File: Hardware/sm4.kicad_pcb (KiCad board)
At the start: 4 copper layers, 65 x 50 mm, 91 parts, among them J1 Motor1, J2 Termination, J3 CAN bus, J4 Motor2, J5 I2C, J6 Power, J7 USB_C_Receptacle_USB2.0, J8 Conn_01x05_Male, Q1 NDT2955, SW1 RST_SW, SW2 BOOT_SW, U1 STM32F412RETx, U2 TMC2100-TA, U3 MCP2562-E-SN, U4 TMC2100-TA, U6 MCP1700-3302E_SOT23, U7 USBLC6-2SC6, Y1 25 MHz

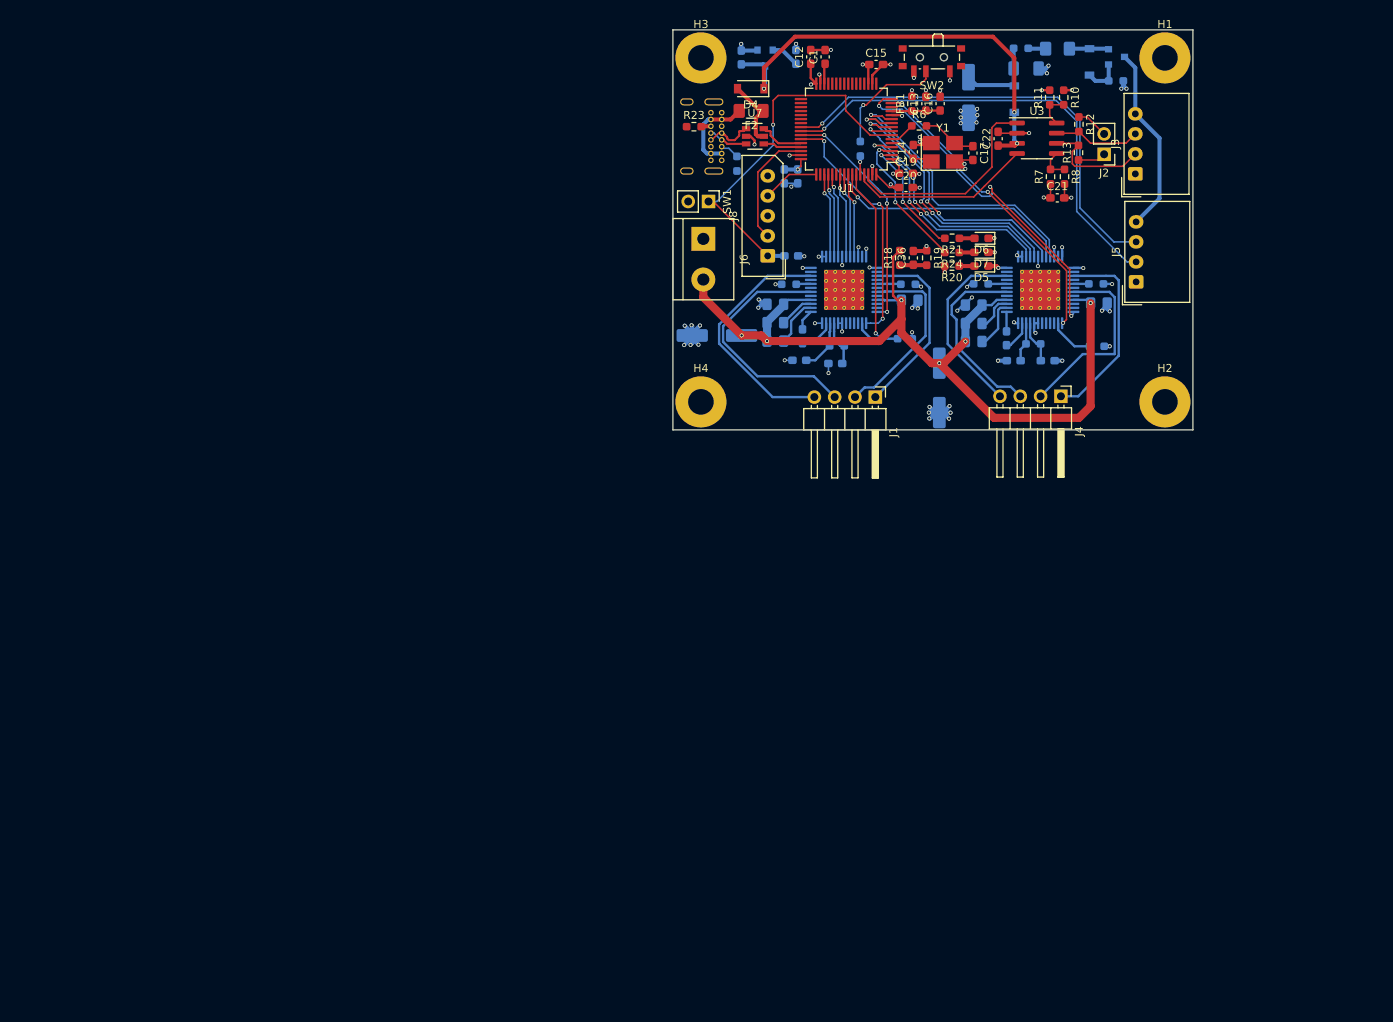
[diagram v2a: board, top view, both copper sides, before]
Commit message: Implement more of the second version of the PCB.
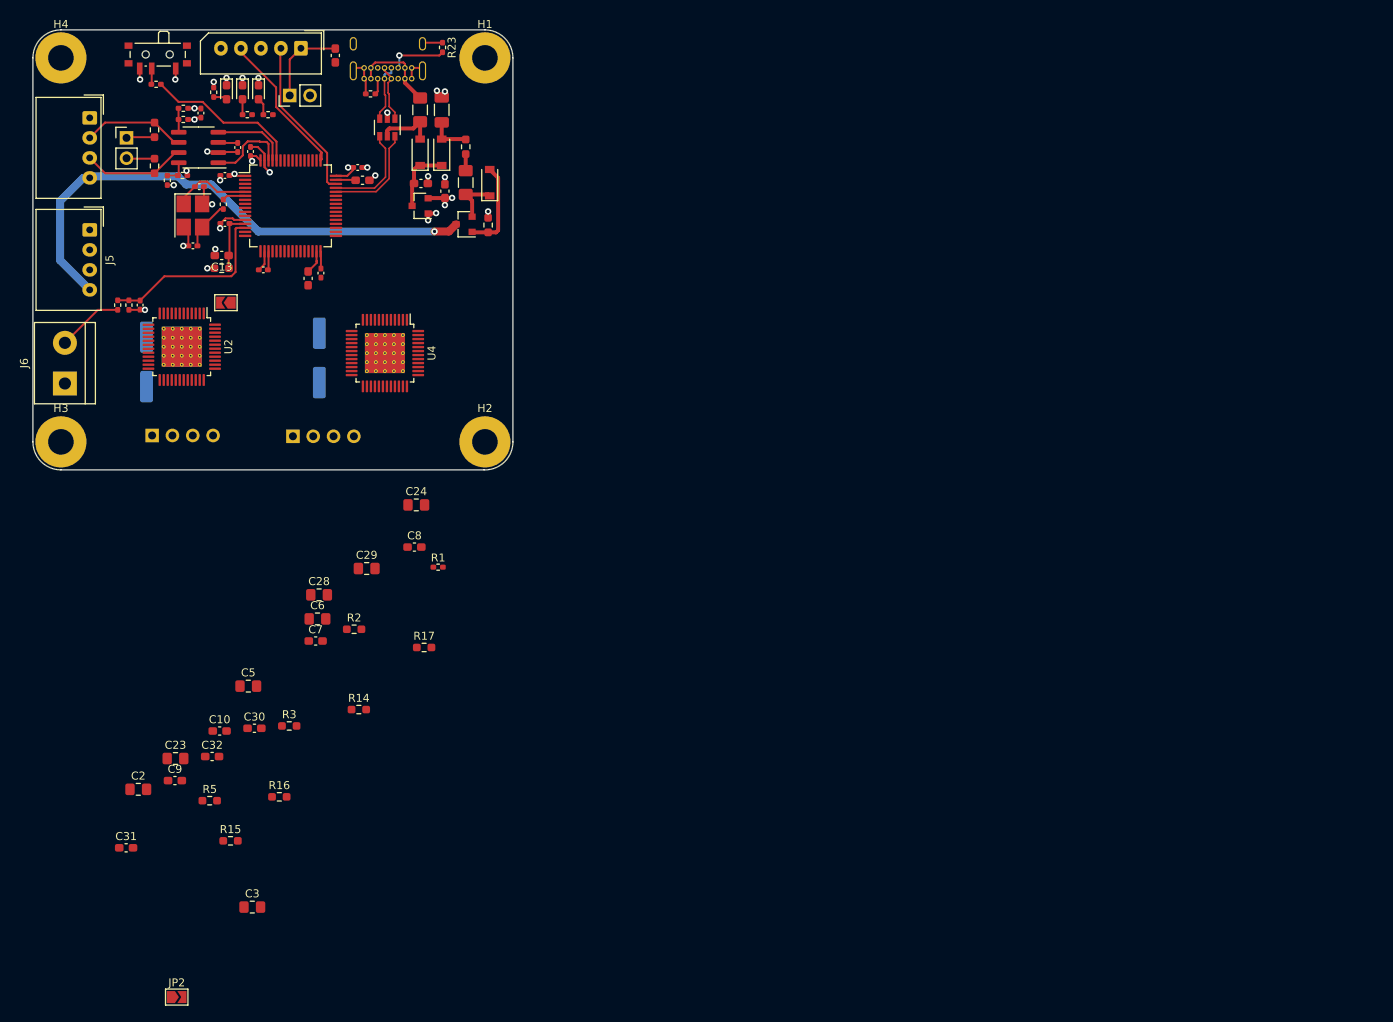
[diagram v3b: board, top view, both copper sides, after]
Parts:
- removed C27: 68u, Capacitor_SMD:C_Elec_6.3x7.7
- added C33: 2u2, Capacitor_SMD:C_0603_1608Metric_Pad1.08x0.95mm_HandSolder, F.Cu at (81.2, 68.8)
- added JP1: Jumper_2_Open, Jumper:SolderJumper-2_P1.3mm_Open_TrianglePad1.0x1.5mm, F.Cu at (64.1, 84.1)
- added JP2: Jumper_2_Open, Jumper:SolderJumper-2_P1.3mm_Open_TrianglePad1.0x1.5mm, F.Cu at (58.0, 170.9)
- C10, C11, C2, C23, C24, C25, C28, C29, C3, C30, C31, C32, C34, C35, C5, C6, C7, C8, C9, D1, D3, F1, FB2, Q1, R14, R15, R16, R17, R2, R3, R5, R9, U2, U4, U6: moved to F.Cu
- C12, C14, C15, C16, C17, C19, C20, C21, C22, C36: footprint Capacitor_SMD:C_0603_1608Metric_Pad1.08x0.95mm_HandSolder -> Capacitor_SMD:C_0402_1005Metric_Pad0.74x0.62mm_HandSolder
- C18: footprint Capacitor_SMD:C_0603_1608Metric_Pad1.08x0.95mm_HandSolder -> Capacitor_SMD:C_0402_1005Metric_Pad0.74x0.62mm_HandSolder; moved to F.Cu
- J1, J4: moved to B.Cu
- R1, R22, R4: footprint Resistor_SMD:R_0603_1608Metric_Pad0.98x0.95mm_HandSolder -> Resistor_SMD:R_0402_1005Metric_Pad0.72x0.64mm_HandSolder; moved to F.Cu
- R10, R11, R18, R19, R20, R21, R23, R24, R6, R7, R8: footprint Resistor_SMD:R_0603_1608Metric_Pad0.98x0.95mm_HandSolder -> Resistor_SMD:R_0402_1005Metric_Pad0.72x0.64mm_HandSolder
- U1: value STM32F412RETx -> STM32F405RGTx
- moved J5 131.0 mm to (47.1, 75.0), turned to 270 degrees
- moved J3 130.9 mm to (47.1, 61.0), turned to 270 degrees
- moved C31 127.2 mm to (51.6, 152.2), turned to 0 degrees
- moved J2 122.2 mm to (51.7, 63.5), turned to 0 degrees
- moved R16 120.6 mm to (70.8, 145.9), turned to 0 degrees
- moved R15 118.0 mm to (64.7, 151.4), turned to 0 degrees
- moved R12 115.7 mm to (55.2, 67.0)
- moved R13 115.5 mm to (55.2, 62.5)
- moved C23 112.6 mm to (57.8, 141.1)
- moved C32 111.8 mm to (62.4, 140.8), turned to 0 degrees
- moved R11 110.8 mm to (56.8, 68.8), turned to 270 degrees
- moved R10 110.6 mm to (58.7, 68.2), turned to 180 degrees
- moved R8 110.5 mm to (58.8, 59.8), turned to 0 degrees
- moved C30 109.3 mm to (67.7, 137.3)
- moved R7 108.6 mm to (58.8, 61.2), turned to 180 degrees
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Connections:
- R21 pad 2: STATUS -> (no net)
- R24 pad 2: ERR -> (no net)
- U1 pad 10: CFG02 -> (no net)
- U1 pad 11: DIR2 -> (no net)
- U1 pad 15: CFG52 -> (no net)
- U1 pad 16: CFG42 -> EN1
- U1 pad 2: STATUS -> (no net)
- U1 pad 20: (no net) -> REF1
- U1 pad 21: (no net) -> REF2
- U1 pad 22: (no net) -> ERR1
- U1 pad 23: (no net) -> MODE1
- U1 pad 29: (no net) -> SCL
- U1 pad 3: ERR -> (no net)
- U1 pad 30: Net-(C1-Pad1) -> SDA
- U1 pad 31: GND -> Net-(C1-Pad1)
- U1 pad 37: (no net) -> STEP1
- U1 pad 38: (no net) -> DIR1
- U1 pad 4: CFG32 -> (no net)
- U1 pad 40: SDA -> (no net)
- U1 pad 41: SCL -> STEP2
- U1 pad 42: CFG41 -> (no net)
- U1 pad 43: CFG51 -> (no net)
- U1 pad 47: GND -> Net-(C33-Pad1)
- U1 pad 51: CFG31 -> (no net)
- U1 pad 52: CFG21 -> (no net)
- U1 pad 53: CFG11 -> (no net)
- U1 pad 55: CFG01 -> (no net)
- U1 pad 56: STEP1 -> (no net)
- U1 pad 57: DIR1 -> (no net)
- U1 pad 58: STEP2 -> (no net)
- U1 pad 59: ERR1 -> (no net)
- U1 pad 8: CFG22 -> (no net)
- U1 pad 9: CFG12 -> (no net)
- U2 pad 24: CFG41 -> GND
- U2 pad 25: CFG51 -> +3V3
- U2 pad 29: (no net) -> EN1
- U2 pad 3: CFG31 -> Net-(JP1-Pad2)
- U2 pad 30: (no net) -> REF1
- U2 pad 4: CFG21 -> (no net)
- U2 pad 5: CFG11 -> MODE1
- U2 pad 7: CFG01 -> GND
- U4 pad 24: CFG42 -> GND
- U4 pad 25: CFG52 -> +3V3
- U4 pad 3: CFG32 -> Net-(JP2-Pad2)
- U4 pad 30: (no net) -> REF2
- U4 pad 4: CFG22 -> (no net)
- U4 pad 5: CFG12 -> MODE1
- U4 pad 7: CFG02 -> GND
- U4 pad 9: DIR2 -> (no net)
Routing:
- net VS1: track 111.1 -> 8.31 mm, vias 6 -> 0
- net GND: track 110.9 -> 51.2 mm, vias 78 -> 24
- net SCL: track 58.5 -> 0.00 mm, vias 1 -> 0
- net SDA: track 57.4 -> 0.00 mm, vias 1 -> 0
- net +5V: track 56.3 -> 10.8 mm, vias 3 -> 0
- net CFG42: track 43.5 -> 0.00 mm, vias 3 -> 0
- net VDC: track 23.6 -> 66.6 mm, vias 0 -> 1
- net CFG52: track 37.9 -> 0.00 mm, vias 3 -> 0
- net NRST: track 47.1 -> 10.8 mm, vias 1 -> 0
- net DIR2: track 35.8 -> 0.00 mm, vias 1 -> 0
- net CFG02: track 35.5 -> 0.00 mm, vias 3 -> 0
- net CFG12: track 33.5 -> 0.00 mm, vias 3 -> 0
- net CFG22: track 31.9 -> 0.00 mm, vias 3 -> 0
- net Net-(J1-Pad4): track 31.8 -> 0.00 mm
- net STEP2: track 31.7 -> 0.00 mm, vias 1 -> 0
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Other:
- board size 65 x 50 mm -> 60 x 55 mm

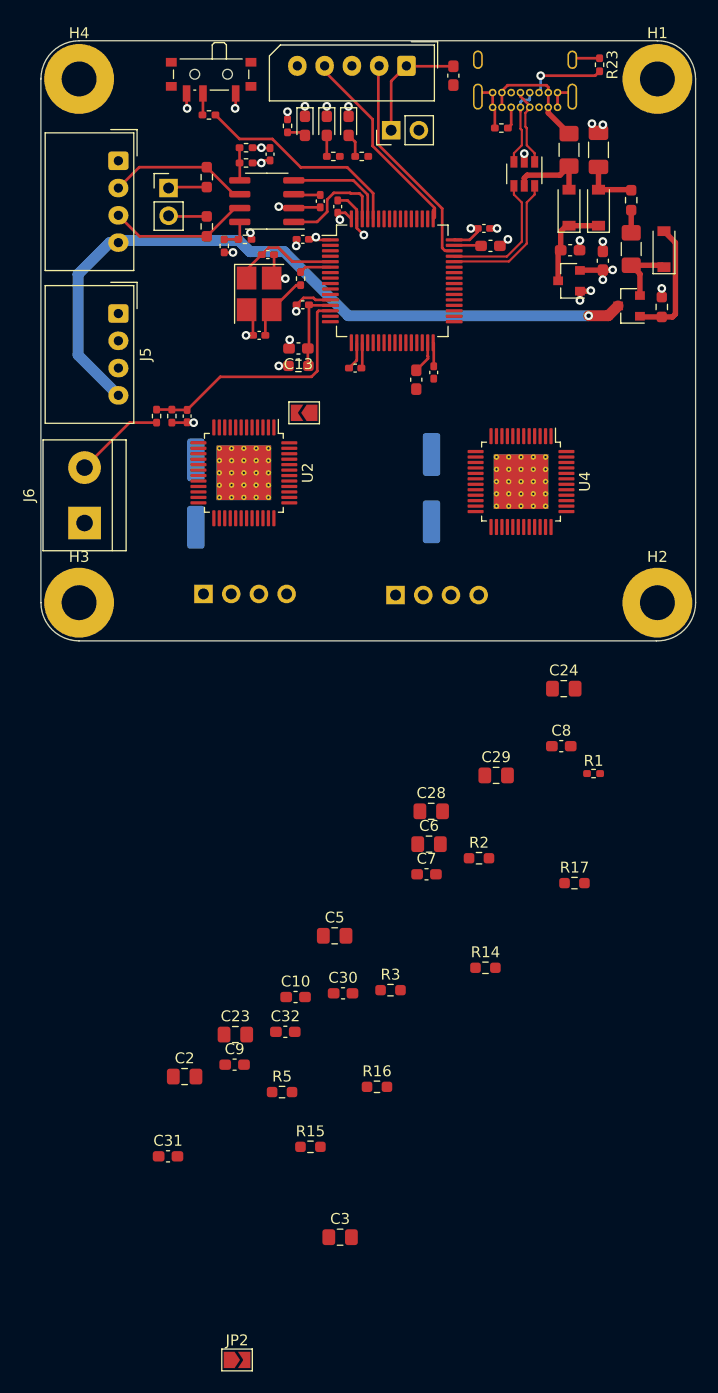
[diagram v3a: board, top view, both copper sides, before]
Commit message: Implement more of the second version of the PCB.
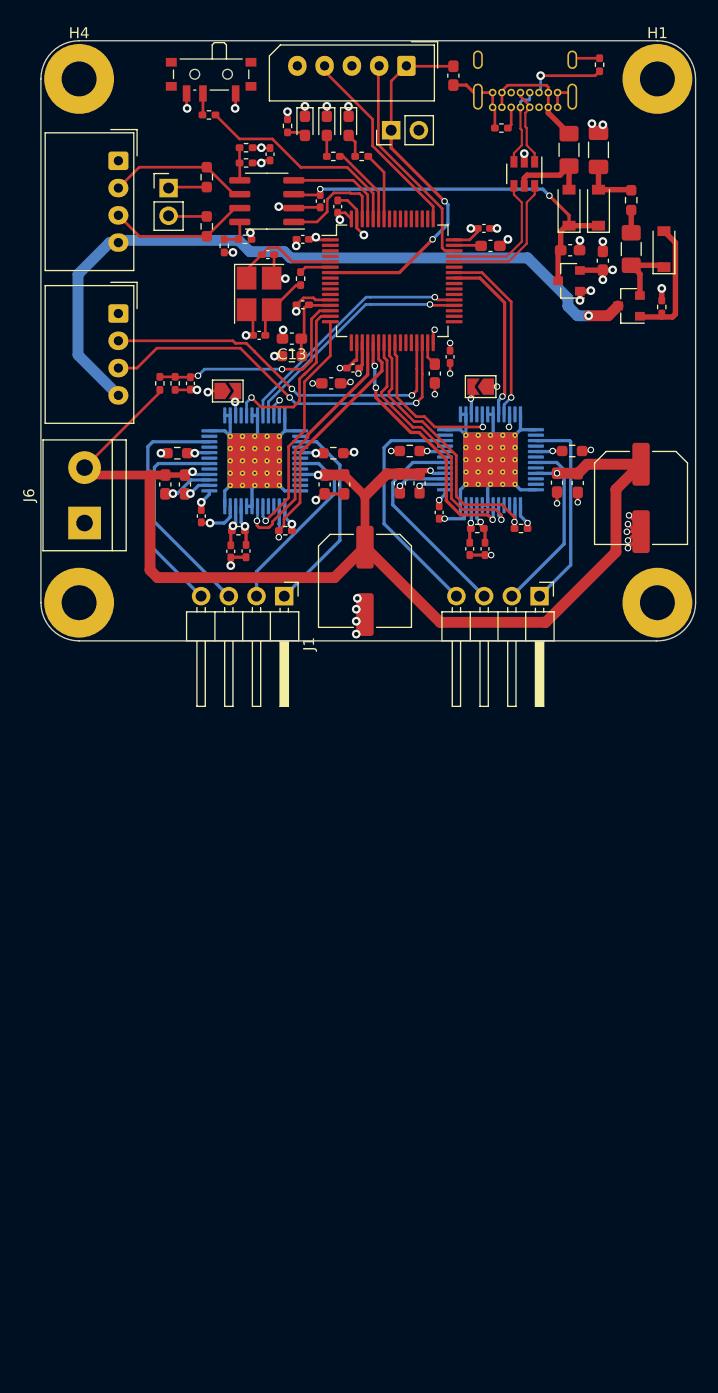
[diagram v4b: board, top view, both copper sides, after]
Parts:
- C10, C30, C31, C32, C7, C9: footprint Capacitor_SMD:C_0603_1608Metric_Pad1.08x0.95mm_HandSolder -> Capacitor_SMD:C_0402_1005Metric_Pad0.74x0.62mm_HandSolder
- C2, C23, C24, C28, C29, C3, C5, C6: footprint Capacitor_SMD:C_0805_2012Metric_Pad1.18x1.45mm_HandSolder -> Capacitor_SMD:C_0603_1608Metric_Pad1.08x0.95mm_HandSolder
- C26, C4, J1, J4: moved to F.Cu
- R14, R15, R2, R9: footprint Resistor_SMD:R_0603_1608Metric_Pad0.98x0.95mm_HandSolder -> Resistor_SMD:R_0402_1005Metric_Pad0.72x0.64mm_HandSolder
- U2, U4: moved to B.Cu
- moved JP2 92.0 mm to (80.3, 81.7), turned to 180 degrees
- moved C3 70.8 mm to (51.4, 90.7), turned to 270 degrees
- moved C31 64.0 mm to (76.5, 93.2), turned to 270 degrees
- moved R16 61.0 mm to (88.7, 87.6), turned to 180 degrees
- moved R5 59.3 mm to (52.5, 87.8)
- moved R15 58.7 mm to (80.0, 94.7), turned to 180 degrees
- moved C2 54.3 mm to (53.2, 90.7), turned to 270 degrees
- moved C23 53.3 mm to (74.7, 90.6), turned to 270 degrees
- moved C9 50.4 mm to (54.7, 93.6), turned to 270 degrees
- moved R3 49.5 mm to (66.8, 87.8), turned to 180 degrees
- moved C32 47.4 mm to (79.3, 96.6), turned to 270 degrees
- moved C30 42.8 mm to (80.7, 96.6), turned to 270 degrees
- moved R17 42.4 mm to (73.8, 87.6)
- moved C5 41.4 mm to (67.8, 90.7), turned to 270 degrees
- moved C10 41.3 mm to (57.4, 96.8), turned to 270 degrees
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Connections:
- R21 pad 2: (no net) -> STATUS
- R24 pad 2: (no net) -> ERR
- U1 pad 15: (no net) -> MODE1
- U1 pad 23: MODE1 -> EN2
- U1 pad 24: (no net) -> ERR2
- U1 pad 25: (no net) -> MODE2
- U1 pad 36: (no net) -> DIR1
- U1 pad 38: DIR1 -> (no net)
- U1 pad 42: (no net) -> DIR2
- U1 pad 58: (no net) -> ERR
- U1 pad 59: (no net) -> STATUS
- U4 pad 29: (no net) -> EN2
- U4 pad 5: MODE1 -> MODE2
- U4 pad 9: (no net) -> DIR2
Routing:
- net VS1: track 8.31 -> 119.5 mm, vias 0 -> 4
- net GND: track 51.2 -> 153.9 mm, vias 24 -> 46
- net SDA: track 0.00 -> 35.9 mm, vias 0 -> 2
- net SCL: track 0.00 -> 34.0 mm, vias 0 -> 2
- net ERR2: track 0.00 -> 26.0 mm, vias 0 -> 1
- net +5V: track 10.8 -> 36.0 mm, vias 0 -> 2
- net ERR1: track 0.00 -> 24.8 mm, vias 0 -> 1
- net EN2: track 0.00 -> 24.8 mm, vias 0 -> 1
- net REF2: track 0.00 -> 24.0 mm, vias 0 -> 3
- net REF1: track 0.00 -> 23.7 mm, vias 0 -> 1
- net NRST: track 10.8 -> 34.2 mm, vias 0 -> 2
- net STEP1: track 0.00 -> 22.9 mm, vias 0 -> 1
- net Net-(J4-Pad4): track 0.00 -> 22.2 mm
- net EN1: track 0.00 -> 22.1 mm, vias 0 -> 1
- net DIR1: track 0.00 -> 22.0 mm, vias 0 -> 1
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
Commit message: Finalize first HW version. Update firmware project.
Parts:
- removed D1: 4V7, Diode_SMD:D_SOD-123
- removed R9: 10k, Resistor_SMD:R_0402_1005Metric_Pad0.72x0.64mm_HandSolder
- added C27: 10u, Capacitor_SMD:C_1206_3216Metric_Pad1.33x1.80mm_HandSolder, F.Cu at (94.9, 85.9)
- added C37: 10u, Capacitor_SMD:C_1206_3216Metric_Pad1.33x1.80mm_HandSolder, F.Cu at (94.9, 93.6)
- added C38: 10u, Capacitor_SMD:C_1206_3216Metric_Pad1.33x1.80mm_HandSolder, F.Cu at (71.5, 103.7)
- added C39: 10u, Capacitor_SMD:C_1206_3216Metric_Pad1.33x1.80mm_HandSolder, F.Cu at (71.6, 96.1)
- added C40: 10u, Capacitor_SMD:C_1206_3216Metric_Pad1.33x1.80mm_HandSolder, F.Cu at (94.9, 96.2)
- added C41: 10u, Capacitor_SMD:C_1206_3216Metric_Pad1.33x1.80mm_HandSolder, F.Cu at (65.8, 98.7)
- added C42: 10u, Capacitor_SMD:C_1206_3216Metric_Pad1.33x1.80mm_HandSolder, F.Cu at (71.5, 98.7)
- added C43: 10u, Capacitor_SMD:C_1206_3216Metric_Pad1.33x1.80mm_HandSolder, F.Cu at (71.5, 101.2)
- added JP3: Jumper_2_Open, Jumper:SolderJumper-2_P1.3mm_Open_TrianglePad1.0x1.5mm, F.Cu at (52.9, 79.0)
- added JP4: Jumper_2_Open, Jumper:SolderJumper-2_P1.3mm_Open_TrianglePad1.0x1.5mm, F.Cu at (56.4, 79.0)
- added R25: 2k2, Resistor_SMD:R_0402_1005Metric_Pad0.72x0.64mm_HandSolder, F.Cu at (52.9, 76.6)
- added R26: 2k2, Resistor_SMD:R_0402_1005Metric_Pad0.72x0.64mm_HandSolder, F.Cu at (56.4, 76.6)
- C26, C4: value 47u -> 10u; footprint Capacitor_SMD:C_Elec_8x6.2 -> Capacitor_SMD:C_1206_3216Metric_Pad1.33x1.80mm_HandSolder
- C30, C7: value 470n -> 4u7; footprint Capacitor_SMD:C_0402_1005Metric_Pad0.74x0.62mm_HandSolder -> Capacitor_SMD:C_0603_1608Metric_Pad1.08x0.95mm_HandSolder
- J1, J4: moved to B.Cu
- Q1: footprint Package_TO_SOT_SMD:SOT-23 -> Package_TO_SOT_SMD:SOT-223-3_TabPin2
- U2, U4: moved to F.Cu
- moved R19 42.4 mm to (94.7, 81.9)
- moved R18 42.4 mm to (93.3, 81.9)
- moved C36 42.4 mm to (96.1, 81.9)
- moved C26 26.6 mm to (94.9, 91.0), turned to 0 degrees
- moved C24 16.2 mm to (89.0, 89.1), turned to 0 degrees
- moved C3 15.7 mm to (67.0, 89.2), turned to 0 degrees
- moved R16 15.3 mm to (73.4, 87.5), turned to 0 degrees
- moved R17 15.2 mm to (89.0, 87.4), turned to 180 degrees
- moved R5 15.0 mm to (67.5, 87.3), turned to 180 degrees
- moved C6 14.7 mm to (51.3, 90.7)
- moved C5 14.7 mm to (53.1, 90.7)
- moved R3 14.6 mm to (52.2, 87.8), turned to 0 degrees
- moved C28 14.3 mm to (73.0, 90.5)
- moved C29 14.3 mm to (74.9, 90.5)
- moved C23 14.0 mm to (88.6, 91.6), turned to 180 degrees
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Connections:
- C24 pad 2: VSA2 -> GND
- C3 pad 2: VSA1 -> GND
- F1 pad 2: Net-(D1-Pad1) -> Net-(F1-Pad2)
- Q1 pad 1: Net-(D1-Pad2) -> GND
- Q1 pad 2: Net-(D1-Pad1) -> VDC
- Q1 pad 3: VDC -> Net-(F1-Pad2)
- U1 pad 14: VBAT -> (no net)
- U1 pad 15: MODE1 -> DIR1
- U1 pad 16: EN1 -> (no net)
- U1 pad 17: (no net) -> MODE1
- U1 pad 22: ERR1 -> EN1
- U1 pad 25: MODE2 -> ERR1
- U1 pad 27: (no net) -> VBAT
- U1 pad 33: (no net) -> DIR2
- U1 pad 36: DIR1 -> (no net)
- U1 pad 42: DIR2 -> MODE2
- U2 pad 39: VSA1 -> VS1
- U4 pad 39: VSA2 -> VS1
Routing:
- net VS1: track 119.5 -> 143.5 mm, vias 4 -> 5
- net Net-(F1-Pad2): track 0.00 -> 23.2 mm
- net Net-(D1-Pad2): track 11.4 -> 0.00 mm
- net VBAT: track 20.4 -> 30.0 mm
- net DIR2: track 16.9 -> 10.0 mm, vias 1 -> 0
- net DIR1: track 22.0 -> 15.5 mm, vias 1 -> 0
- net Net-(D1-Pad1): track 6.18 -> 0.00 mm
- net VDC: track 67.1 -> 73.1 mm
- net REF2: track 24.0 -> 29.8 mm, vias 3 -> 2
- net Net-(J4-Pad4): track 22.2 -> 17.0 mm, vias 0 -> 1
- net Net-(C17-Pad1): track 6.17 -> 11.2 mm
- net VSA2: track 5.03 -> 0.00 mm, vias 1 -> 0
- net VSA1: track 4.57 -> 0.00 mm, vias 1 -> 0
- net MODE1: track 16.3 -> 11.8 mm, vias 1 -> 0
- net GND: track 153.9 -> 149.5 mm, vias 46 -> 286
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- added copper zone on B.Cu, net GND
- added copper zone on F.Cu, net GND
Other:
- board size 60 x 55 mm -> 65 x 56 mm
